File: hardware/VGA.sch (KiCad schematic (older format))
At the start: 12 parts

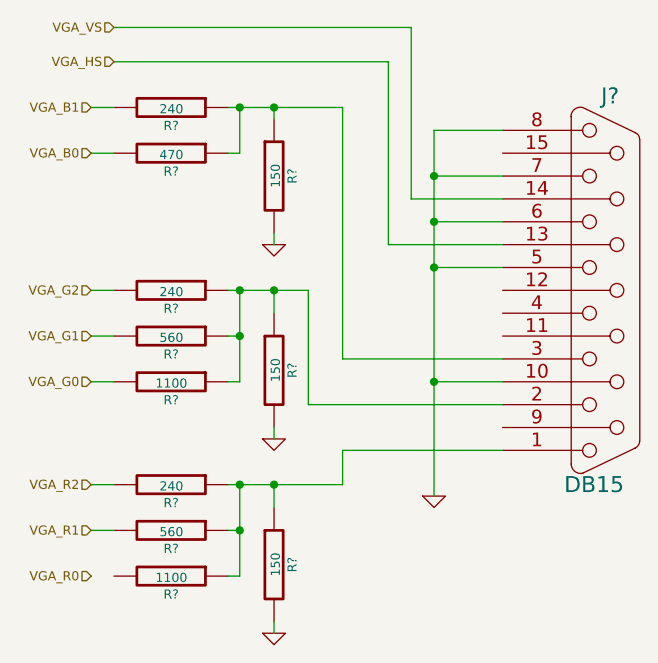
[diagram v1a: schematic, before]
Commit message: Se agrego alimentacion por USB-Serie, falta fuente
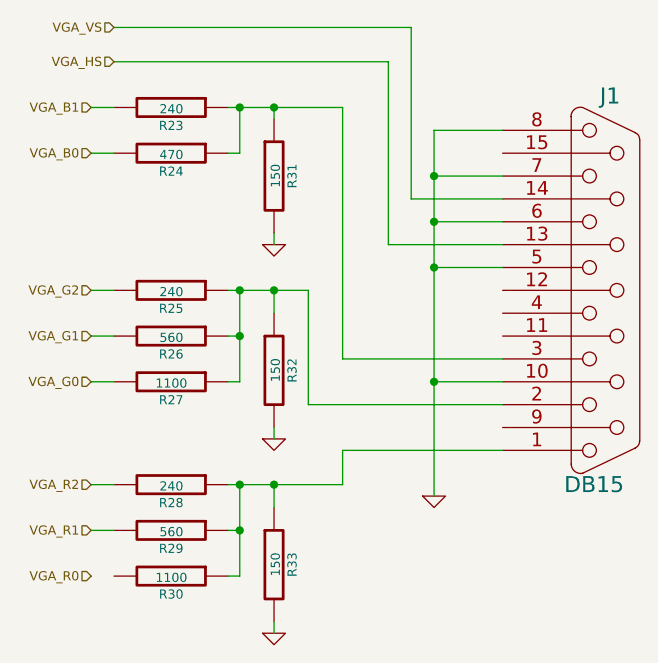
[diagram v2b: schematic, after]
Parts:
- gave numbers to parts that had none: 12
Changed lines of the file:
@@
 $Descr A4 11693 8268
 encoding utf-8
-Sheet 3 4
+Sheet 3 5
 Title ""
 Date ""
@@
 $EndDescr
 $Comp
-L DB15 J?
+L DB15 J1
 U 1 1 538FEAA4
 P 4700 2450
-F 0 "J?" H 4720 3300 70  0000 C CNN
+F 0 "J1" H 4720 3300 70  0000 C CNN
 F 1 "DB15" H 4650 1600 70  0000 C CNN
 F 2 "" H 4700 2450 60  0000 C CNN
@@
 $EndComp
 $Comp
-L R R?
+L R R32
 U 1 1 538FEB0B
 P 3250 2800
-F 0 "R?" V 3330 2800 40  0000 C CNN
+F 0 "R32" V 3330 2800 40  0000 C CNN
 F 1 "150" V 3257 2801 40  0000 C CNN
 F 2 "" V 3180 2800 30  0000 C CNN
@@
 $EndComp
 $Comp
-L R R?
+L R R25
 U 1 1 538FED58
 P 2800 2450
-F 0 "R?" V 2880 2450 40  0000 C CNN
+F 0 "R25" V 2880 2450 40  0000 C CNN
 F 1 "240" V 2807 2451 40  0000 C CNN
 F 2 "" V 2730 2450 30  0000 C CNN
@@
 $EndComp
 $Comp
-L R R?
+L R R26
 U 1 1 538FEDA0
 P 2800 2650
-F 0 "R?" V 2880 2650 40  0000 C CNN
+F 0 "R26" V 2880 2650 40  0000 C CNN
 F 1 "560" V 2807 2651 40  0000 C CNN
 F 2 "" V 2730 2650 30  0000 C CNN
@@
 $EndComp
 $Comp
-L R R?
+L R R27
 U 1 1 538FEDC2
 P 2800 2850
-F 0 "R?" V 2880 2850 40  0000 C CNN
+F 0 "R27" V 2880 2850 40  0000 C CNN
 F 1 "1100" V 2807 2851 40  0000 C CNN
 F 2 "" V 2730 2850 30  0000 C CNN
@@
 $EndComp
 $Comp
-L R R?
+L R R33
 U 1 1 538FEED3
 P 3250 3650
-F 0 "R?" V 3330 3650 40  0000 C CNN
+F 0 "R33" V 3330 3650 40  0000 C CNN
 F 1 "150" V 3257 3651 40  0000 C CNN
 F 2 "" V 3180 3650 30  0000 C CNN
@@
 $EndComp
 $Comp
-L R R?
+L R R28
 U 1 1 538FEED9
 P 2800 3300
-F 0 "R?" V 2880 3300 40  0000 C CNN
+F 0 "R28" V 2880 3300 40  0000 C CNN
 F 1 "240" V 2807 3301 40  0000 C CNN
 F 2 "" V 2730 3300 30  0000 C CNN
@@
 $EndComp
 $Comp
-L R R?
+L R R29
 U 1 1 538FEEDF
 P 2800 3500
-F 0 "R?" V 2880 3500 40  0000 C CNN
+F 0 "R29" V 2880 3500 40  0000 C CNN
 F 1 "560" V 2807 3501 40  0000 C CNN
 F 2 "" V 2730 3500 30  0000 C CNN
@@
 $EndComp
 $Comp
-L R R?
+L R R30
 U 1 1 538FEEE5
 P 2800 3700
-F 0 "R?" V 2880 3700 40  0000 C CNN
+F 0 "R30" V 2880 3700 40  0000 C CNN
 F 1 "1100" V 2807 3701 40  0000 C CNN
 F 2 "" V 2730 3700 30  0000 C CNN
@@
 $EndComp
 $Comp
-L GND #PWR?
+L GND #PWR35
 U 1 1 538FEEF6
 P 3950 3350
-F 0 "#PWR?" H 3950 3350 30  0001 C CNN
+F 0 "#PWR35" H 3950 3350 30  0001 C CNN
 F 1 "GND" H 3950 3280 30  0001 C CNN
 F 2 "" H 3950 3350 60  0000 C CNN
@@
 Connection ~ 3950 2350
 $Comp
-L R R?
+L R R31
 U 1 1 538FF276
 P 3250 1950
-F 0 "R?" V 3330 1950 40  0000 C CNN
+F 0 "R31" V 3330 1950 40  0000 C CNN
 F 1 "150" V 3257 1951 40  0000 C CNN
 F 2 "" V 3180 1950 30  0000 C CNN
@@
 $EndComp
 $Comp
-L R R?
+L R R23
 U 1 1 538FF27C
 P 2800 1650
-F 0 "R?" V 2880 1650 40  0000 C CNN
+F 0 "R23" V 2880 1650 40  0000 C CNN
 F 1 "240" V 2807 1651 40  0000 C CNN
 F 2 "" V 2730 1650 30  0000 C CNN
@@
 $EndComp
 $Comp
-L R R?
+L R R24
 U 1 1 538FF282
 P 2800 1850
-F 0 "R?" V 2880 1850 40  0000 C CNN
+F 0 "R24" V 2880 1850 40  0000 C CNN
 F 1 "470" V 2807 1851 40  0000 C CNN
 F 2 "" V 2730 1850 30  0000 C CNN
@@
 Connection ~ 3100 3300
 $Comp
-L GND #PWR?
+L GND #PWR34
 U 1 1 538FF446
 P 3250 3950
-F 0 "#PWR?" H 3250 3950 30  0001 C CNN
+F 0 "#PWR34" H 3250 3950 30  0001 C CNN
 F 1 "GND" H 3250 3880 30  0001 C CNN
 F 2 "" H 3250 3950 60  0000 C CNN
@@
 $EndComp
 $Comp
-L GND #PWR?
+L GND #PWR33
 U 1 1 538FF45D
 P 3250 3100
-F 0 "#PWR?" H 3250 3100 30  0001 C CNN
+F 0 "#PWR33" H 3250 3100 30  0001 C CNN
 F 1 "GND" H 3250 3030 30  0001 C CNN
 F 2 "" H 3250 3100 60  0000 C CNN
@@
 $EndComp
 $Comp
-L GND #PWR?
+L GND #PWR32
 U 1 1 538FF474
 P 3250 2250
-F 0 "#PWR?" H 3250 2250 30  0001 C CNN
+F 0 "#PWR32" H 3250 2250 30  0001 C CNN
 F 1 "GND" H 3250 2180 30  0001 C CNN
 F 2 "" H 3250 2250 60  0000 C CNN

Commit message: Se agrego SD, se colocaron pins en varios modulos, se corrigio orden del VGA
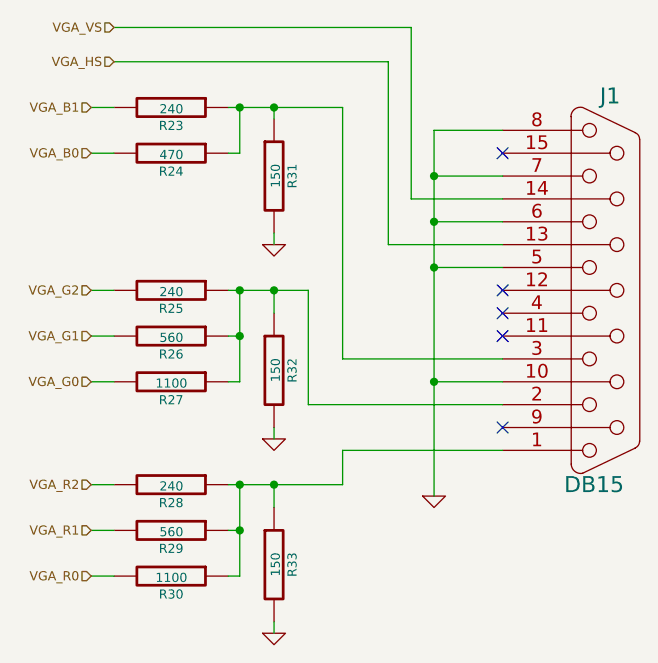
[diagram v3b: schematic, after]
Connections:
- net VGA_R0: now also R30.2
- no-connect marks 0 -> 5
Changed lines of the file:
@@
 LIBS:serial
 LIBS:oscillator-cmos-out-4
+LIBS:con-yamaichi-cf-2
 LIBS:STM32F4-UCC-cache
 EELAYER 24 0
@@
 $Descr A4 11693 8268
 encoding utf-8
-Sheet 3 5
+Sheet 3 6
 Title ""
 Date ""
@@
 Wire Wire Line
 	2550 3500 2450 3500
+Wire Wire Line
+	2550 3700 2450 3700
+NoConn ~ 4250 1850
+NoConn ~ 4250 2450
+NoConn ~ 4250 2550
+NoConn ~ 4250 2650
+NoConn ~ 4250 3050
 $EndSCHEMATC

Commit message: Terminado el esquematico, iniciado el PCB
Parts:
- R23, R24, R25, R26, R27, R28, R29, R30, R31, R32, R33: footprint (none) -> Resistors_SMD:Resistor_SMD1206_ReflowWave
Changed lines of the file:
@@
 F 0 "J1" H 4720 3300 70  0000 C CNN
 F 1 "DB15" H 4650 1600 70  0000 C CNN
-F 2 "" H 4700 2450 60  0000 C CNN
+F 2 "" H 4700 2450 60  0001 C CNN
 F 3 "" H 4700 2450 60  0000 C CNN
 	1    4700 2450
@@
 F 0 "R32" V 3330 2800 40  0000 C CNN
 F 1 "150" V 3257 2801 40  0000 C CNN
-F 2 "" V 3180 2800 30  0000 C CNN
+F 2 "Resistors_SMD:Resistor_SMD1206_ReflowWave" V 3180 2800 30  0001 C CNN
 F 3 "" H 3250 2800 30  0000 C CNN
 	1    3250 2800
@@
 F 0 "R25" V 2880 2450 40  0000 C CNN
 F 1 "240" V 2807 2451 40  0000 C CNN
-F 2 "" V 2730 2450 30  0000 C CNN
+F 2 "Resistors_SMD:Resistor_SMD1206_ReflowWave" V 2730 2450 30  0001 C CNN
 F 3 "" H 2800 2450 30  0000 C CNN
 	1    2800 2450
@@
 F 0 "R26" V 2880 2650 40  0000 C CNN
 F 1 "560" V 2807 2651 40  0000 C CNN
-F 2 "" V 2730 2650 30  0000 C CNN
+F 2 "Resistors_SMD:Resistor_SMD1206_ReflowWave" V 2730 2650 30  0001 C CNN
 F 3 "" H 2800 2650 30  0000 C CNN
 	1    2800 2650
@@
 F 0 "R27" V 2880 2850 40  0000 C CNN
 F 1 "1100" V 2807 2851 40  0000 C CNN
-F 2 "" V 2730 2850 30  0000 C CNN
+F 2 "Resistors_SMD:Resistor_SMD1206_ReflowWave" V 2730 2850 30  0001 C CNN
 F 3 "" H 2800 2850 30  0000 C CNN
 	1    2800 2850
@@
 F 0 "R33" V 3330 3650 40  0000 C CNN
 F 1 "150" V 3257 3651 40  0000 C CNN
-F 2 "" V 3180 3650 30  0000 C CNN
+F 2 "Resistors_SMD:Resistor_SMD1206_ReflowWave" V 3180 3650 30  0001 C CNN
 F 3 "" H 3250 3650 30  0000 C CNN
 	1    3250 3650
@@
 F 0 "R28" V 2880 3300 40  0000 C CNN
 F 1 "240" V 2807 3301 40  0000 C CNN
-F 2 "" V 2730 3300 30  0000 C CNN
+F 2 "Resistors_SMD:Resistor_SMD1206_ReflowWave" V 2730 3300 30  0001 C CNN
 F 3 "" H 2800 3300 30  0000 C CNN
 	1    2800 3300
@@
 F 0 "R29" V 2880 3500 40  0000 C CNN
 F 1 "560" V 2807 3501 40  0000 C CNN
-F 2 "" V 2730 3500 30  0000 C CNN
+F 2 "Resistors_SMD:Resistor_SMD1206_ReflowWave" V 2730 3500 30  0001 C CNN
 F 3 "" H 2800 3500 30  0000 C CNN
 	1    2800 3500
@@
 F 0 "R30" V 2880 3700 40  0000 C CNN
 F 1 "1100" V 2807 3701 40  0000 C CNN
-F 2 "" V 2730 3700 30  0000 C CNN
+F 2 "Resistors_SMD:Resistor_SMD1206_ReflowWave" V 2730 3700 30  0001 C CNN
 F 3 "" H 2800 3700 30  0000 C CNN
 	1    2800 3700
@@
 $EndComp
 $Comp
-L GND #PWR35
+L GND #PWR030
 U 1 1 538FEEF6
 P 3950 3350
-F 0 "#PWR35" H 3950 3350 30  0001 C CNN
+F 0 "#PWR030" H 3950 3350 30  0001 C CNN
 F 1 "GND" H 3950 3280 30  0001 C CNN
 F 2 "" H 3950 3350 60  0000 C CNN
@@
 F 0 "R31" V 3330 1950 40  0000 C CNN
 F 1 "150" V 3257 1951 40  0000 C CNN
-F 2 "" V 3180 1950 30  0000 C CNN
+F 2 "Resistors_SMD:Resistor_SMD1206_ReflowWave" V 3180 1950 30  0001 C CNN
 F 3 "" H 3250 1950 30  0000 C CNN
 	1    3250 1950
@@
 F 0 "R23" V 2880 1650 40  0000 C CNN
 F 1 "240" V 2807 1651 40  0000 C CNN
-F 2 "" V 2730 1650 30  0000 C CNN
+F 2 "Resistors_SMD:Resistor_SMD1206_ReflowWave" V 2730 1650 30  0001 C CNN
 F 3 "" H 2800 1650 30  0000 C CNN
 	1    2800 1650
@@
 F 0 "R24" V 2880 1850 40  0000 C CNN
 F 1 "470" V 2807 1851 40  0000 C CNN
-F 2 "" V 2730 1850 30  0000 C CNN
+F 2 "Resistors_SMD:Resistor_SMD1206_ReflowWave" V 2730 1850 30  0001 C CNN
 F 3 "" H 2800 1850 30  0000 C CNN
 	1    2800 1850
@@
 Connection ~ 3100 3300
 $Comp
-L GND #PWR34
+L GND #PWR031
 U 1 1 538FF446
 P 3250 3950
-F 0 "#PWR34" H 3250 3950 30  0001 C CNN
+F 0 "#PWR031" H 3250 3950 30  0001 C CNN
 F 1 "GND" H 3250 3880 30  0001 C CNN
 F 2 "" H 3250 3950 60  0000 C CNN
@@
 $EndComp
 $Comp
-L GND #PWR33
+L GND #PWR032
 U 1 1 538FF45D
 P 3250 3100
-F 0 "#PWR33" H 3250 3100 30  0001 C CNN
+F 0 "#PWR032" H 3250 3100 30  0001 C CNN
 F 1 "GND" H 3250 3030 30  0001 C CNN
 F 2 "" H 3250 3100 60  0000 C CNN
@@
 $EndComp
 $Comp
-L GND #PWR32
+L GND #PWR033
 U 1 1 538FF474
 P 3250 2250
-F 0 "#PWR32" H 3250 2250 30  0001 C CNN
+F 0 "#PWR033" H 3250 2250 30  0001 C CNN
 F 1 "GND" H 3250 2180 30  0001 C CNN
 F 2 "" H 3250 2250 60  0000 C CNN

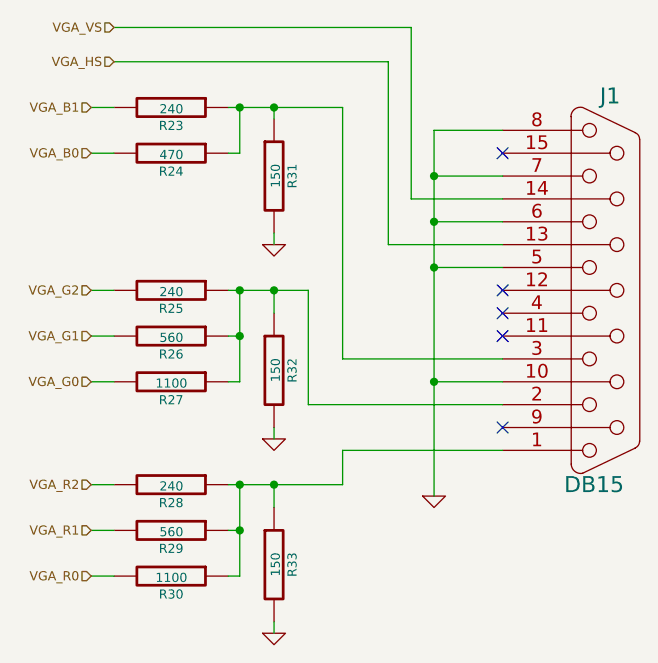
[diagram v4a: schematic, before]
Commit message: Terminado el Routeo de la Placa
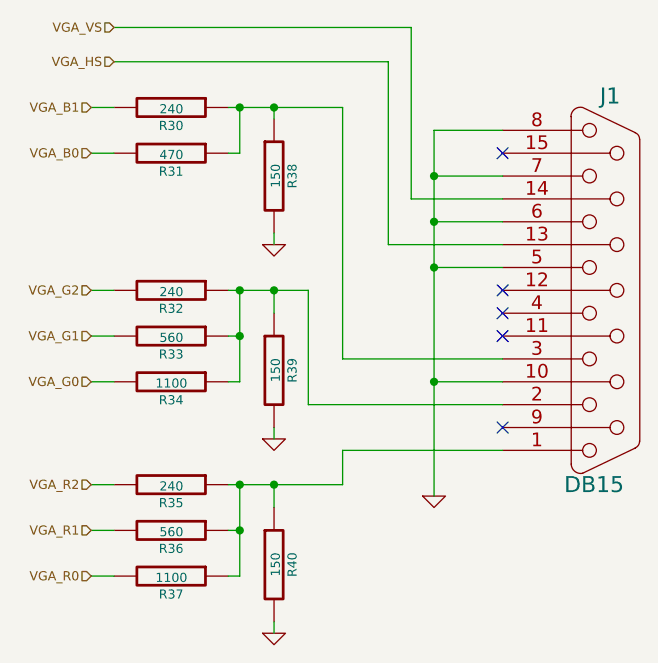
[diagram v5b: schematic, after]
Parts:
- J1: footprint (none) -> w_conn_pc:DB_15F-VGA
- R30: renamed from R23; footprint Resistors_SMD:Resistor_SMD1206_ReflowWave -> Resistors_SMD:R_0805
- R31: renamed from R24; footprint Resistors_SMD:Resistor_SMD1206_ReflowWave -> Resistors_SMD:R_0805
- R32: renamed from R25; footprint Resistors_SMD:Resistor_SMD1206_ReflowWave -> Resistors_SMD:R_0805
- R33: renamed from R26; footprint Resistors_SMD:Resistor_SMD1206_ReflowWave -> Resistors_SMD:R_0805
- R34: renamed from R27; footprint Resistors_SMD:Resistor_SMD1206_ReflowWave -> Resistors_SMD:R_0805
- R35: renamed from R28; footprint Resistors_SMD:Resistor_SMD1206_ReflowWave -> Resistors_SMD:R_0805
- R36: renamed from R29; footprint Resistors_SMD:Resistor_SMD1206_ReflowWave -> Resistors_SMD:R_0805
- R37: renamed from R30; footprint Resistors_SMD:Resistor_SMD1206_ReflowWave -> Resistors_SMD:R_0805
- R38: renamed from R31; footprint Resistors_SMD:Resistor_SMD1206_ReflowWave -> Resistors_SMD:R_0805
- R39: renamed from R32; footprint Resistors_SMD:Resistor_SMD1206_ReflowWave -> Resistors_SMD:R_0805
- R40: renamed from R33; footprint Resistors_SMD:Resistor_SMD1206_ReflowWave -> Resistors_SMD:R_0805
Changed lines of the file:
@@
 LIBS:oscillator-cmos-out-4
 LIBS:con-yamaichi-cf-2
+LIBS:w_connectors
 LIBS:STM32F4-UCC-cache
 EELAYER 24 0
@@
 F 0 "J1" H 4720 3300 70  0000 C CNN
 F 1 "DB15" H 4650 1600 70  0000 C CNN
-F 2 "" H 4700 2450 60  0001 C CNN
+F 2 "w_conn_pc:DB_15F-VGA" H 4700 2450 60  0001 C CNN
 F 3 "" H 4700 2450 60  0000 C CNN
 	1    4700 2450
@@
 $EndComp
 $Comp
-L R R32
+L R R39
 U 1 1 538FEB0B
 P 3250 2800
-F 0 "R32" V 3330 2800 40  0000 C CNN
+F 0 "R39" V 3330 2800 40  0000 C CNN
 F 1 "150" V 3257 2801 40  0000 C CNN
-F 2 "Resistors_SMD:Resistor_SMD1206_ReflowWave" V 3180 2800 30  0001 C CNN
+F 2 "Resistors_SMD:R_0805" V 3180 2800 30  0001 C CNN
 F 3 "" H 3250 2800 30  0000 C CNN
 	1    3250 2800
@@
 $EndComp
 $Comp
-L R R25
+L R R32
 U 1 1 538FED58
 P 2800 2450
-F 0 "R25" V 2880 2450 40  0000 C CNN
+F 0 "R32" V 2880 2450 40  0000 C CNN
 F 1 "240" V 2807 2451 40  0000 C CNN
-F 2 "Resistors_SMD:Resistor_SMD1206_ReflowWave" V 2730 2450 30  0001 C CNN
+F 2 "Resistors_SMD:R_0805" V 2730 2450 30  0001 C CNN
 F 3 "" H 2800 2450 30  0000 C CNN
 	1    2800 2450
@@
 $EndComp
 $Comp
-L R R26
+L R R33
 U 1 1 538FEDA0
 P 2800 2650
-F 0 "R26" V 2880 2650 40  0000 C CNN
+F 0 "R33" V 2880 2650 40  0000 C CNN
 F 1 "560" V 2807 2651 40  0000 C CNN
-F 2 "Resistors_SMD:Resistor_SMD1206_ReflowWave" V 2730 2650 30  0001 C CNN
+F 2 "Resistors_SMD:R_0805" V 2730 2650 30  0001 C CNN
 F 3 "" H 2800 2650 30  0000 C CNN
 	1    2800 2650
@@
 $EndComp
 $Comp
-L R R27
+L R R34
 U 1 1 538FEDC2
 P 2800 2850
-F 0 "R27" V 2880 2850 40  0000 C CNN
+F 0 "R34" V 2880 2850 40  0000 C CNN
 F 1 "1100" V 2807 2851 40  0000 C CNN
-F 2 "Resistors_SMD:Resistor_SMD1206_ReflowWave" V 2730 2850 30  0001 C CNN
+F 2 "Resistors_SMD:R_0805" V 2730 2850 30  0001 C CNN
 F 3 "" H 2800 2850 30  0000 C CNN
 	1    2800 2850
@@
 $EndComp
 $Comp
-L R R33
+L R R40
 U 1 1 538FEED3
 P 3250 3650
-F 0 "R33" V 3330 3650 40  0000 C CNN
+F 0 "R40" V 3330 3650 40  0000 C CNN
 F 1 "150" V 3257 3651 40  0000 C CNN
-F 2 "Resistors_SMD:Resistor_SMD1206_ReflowWave" V 3180 3650 30  0001 C CNN
+F 2 "Resistors_SMD:R_0805" V 3180 3650 30  0001 C CNN
 F 3 "" H 3250 3650 30  0000 C CNN
 	1    3250 3650
@@
 $EndComp
 $Comp
-L R R28
+L R R35
 U 1 1 538FEED9
 P 2800 3300
-F 0 "R28" V 2880 3300 40  0000 C CNN
+F 0 "R35" V 2880 3300 40  0000 C CNN
 F 1 "240" V 2807 3301 40  0000 C CNN
-F 2 "Resistors_SMD:Resistor_SMD1206_ReflowWave" V 2730 3300 30  0001 C CNN
+F 2 "Resistors_SMD:R_0805" V 2730 3300 30  0001 C CNN
 F 3 "" H 2800 3300 30  0000 C CNN
 	1    2800 3300
@@
 $EndComp
 $Comp
-L R R29
+L R R36
 U 1 1 538FEEDF
 P 2800 3500
-F 0 "R29" V 2880 3500 40  0000 C CNN
+F 0 "R36" V 2880 3500 40  0000 C CNN
 F 1 "560" V 2807 3501 40  0000 C CNN
-F 2 "Resistors_SMD:Resistor_SMD1206_ReflowWave" V 2730 3500 30  0001 C CNN
+F 2 "Resistors_SMD:R_0805" V 2730 3500 30  0001 C CNN
 F 3 "" H 2800 3500 30  0000 C CNN
 	1    2800 3500
@@
 $EndComp
 $Comp
-L R R30
+L R R37
 U 1 1 538FEEE5
 P 2800 3700
-F 0 "R30" V 2880 3700 40  0000 C CNN
+F 0 "R37" V 2880 3700 40  0000 C CNN
 F 1 "1100" V 2807 3701 40  0000 C CNN
-F 2 "Resistors_SMD:Resistor_SMD1206_ReflowWave" V 2730 3700 30  0001 C CNN
+F 2 "Resistors_SMD:R_0805" V 2730 3700 30  0001 C CNN
 F 3 "" H 2800 3700 30  0000 C CNN
 	1    2800 3700
@@
 $EndComp
 $Comp
-L GND #PWR030
+L GND #PWR023
 U 1 1 538FEEF6
 P 3950 3350
-F 0 "#PWR030" H 3950 3350 30  0001 C CNN
+F 0 "#PWR023" H 3950 3350 30  0001 C CNN
 F 1 "GND" H 3950 3280 30  0001 C CNN
 F 2 "" H 3950 3350 60  0000 C CNN
@@
 Connection ~ 3950 2350
 $Comp
-L R R31
+L R R38
 U 1 1 538FF276
 P 3250 1950
-F 0 "R31" V 3330 1950 40  0000 C CNN
+F 0 "R38" V 3330 1950 40  0000 C CNN
 F 1 "150" V 3257 1951 40  0000 C CNN
-F 2 "Resistors_SMD:Resistor_SMD1206_ReflowWave" V 3180 1950 30  0001 C CNN
+F 2 "Resistors_SMD:R_0805" V 3180 1950 30  0001 C CNN
 F 3 "" H 3250 1950 30  0000 C CNN
 	1    3250 1950
@@
 $EndComp
 $Comp
-L R R23
+L R R30
 U 1 1 538FF27C
 P 2800 1650
-F 0 "R23" V 2880 1650 40  0000 C CNN
+F 0 "R30" V 2880 1650 40  0000 C CNN
 F 1 "240" V 2807 1651 40  0000 C CNN
-F 2 "Resistors_SMD:Resistor_SMD1206_ReflowWave" V 2730 1650 30  0001 C CNN
+F 2 "Resistors_SMD:R_0805" V 2730 1650 30  0001 C CNN
 F 3 "" H 2800 1650 30  0000 C CNN
 	1    2800 1650
@@
 $EndComp
 $Comp
-L R R24
+L R R31
 U 1 1 538FF282
 P 2800 1850
-F 0 "R24" V 2880 1850 40  0000 C CNN
+F 0 "R31" V 2880 1850 40  0000 C CNN
 F 1 "470" V 2807 1851 40  0000 C CNN
-F 2 "Resistors_SMD:Resistor_SMD1206_ReflowWave" V 2730 1850 30  0001 C CNN
+F 2 "Resistors_SMD:R_0805" V 2730 1850 30  0001 C CNN
 F 3 "" H 2800 1850 30  0000 C CNN
 	1    2800 1850
@@
 Connection ~ 3100 3300
 $Comp
-L GND #PWR031
+L GND #PWR024
 U 1 1 538FF446
 P 3250 3950
-F 0 "#PWR031" H 3250 3950 30  0001 C CNN
+F 0 "#PWR024" H 3250 3950 30  0001 C CNN
 F 1 "GND" H 3250 3880 30  0001 C CNN
 F 2 "" H 3250 3950 60  0000 C CNN
@@
 $EndComp
 $Comp
-L GND #PWR032
+L GND #PWR025
 U 1 1 538FF45D
 P 3250 3100
-F 0 "#PWR032" H 3250 3100 30  0001 C CNN
+F 0 "#PWR025" H 3250 3100 30  0001 C CNN
 F 1 "GND" H 3250 3030 30  0001 C CNN
 F 2 "" H 3250 3100 60  0000 C CNN
@@
 $EndComp
 $Comp
-L GND #PWR033
+L GND #PWR026
 U 1 1 538FF474
 P 3250 2250
-F 0 "#PWR033" H 3250 2250 30  0001 C CNN
+F 0 "#PWR026" H 3250 2250 30  0001 C CNN
 F 1 "GND" H 3250 2180 30  0001 C CNN
 F 2 "" H 3250 2250 60  0000 C CNN
